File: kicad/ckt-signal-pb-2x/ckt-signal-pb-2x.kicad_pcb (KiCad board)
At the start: 2 copper layers, 25.8 x 66.7 mm, 15 parts, among them J1 Molex 0532610471, J2 Molex 0532610471

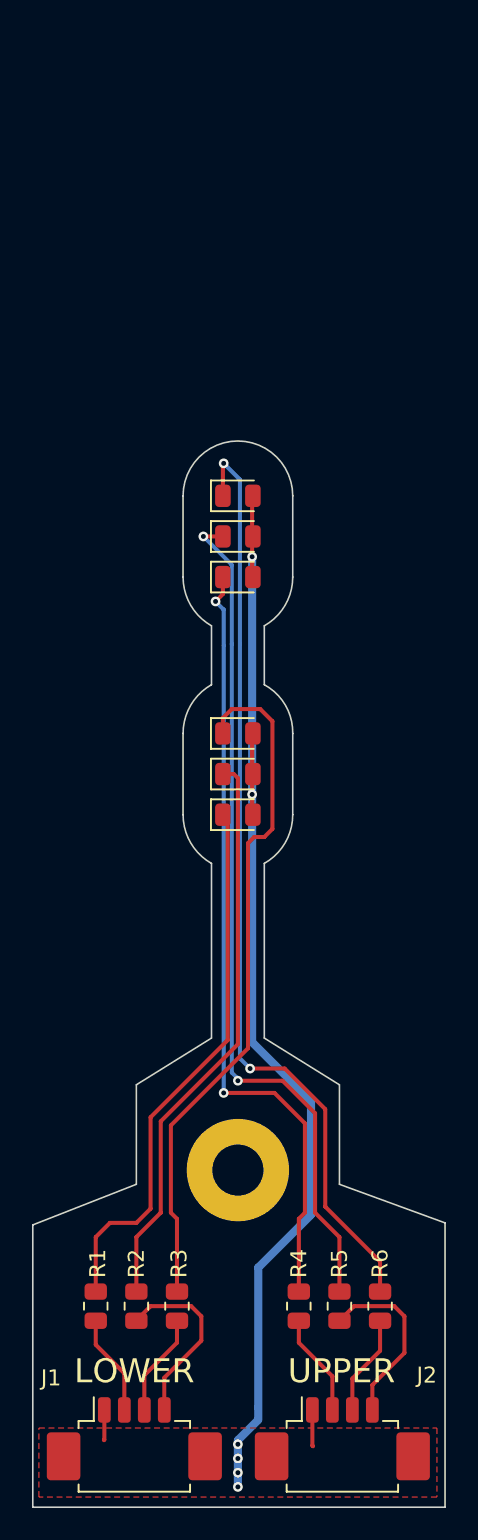
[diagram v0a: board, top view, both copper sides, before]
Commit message: Cleanup pcb, rename preference file
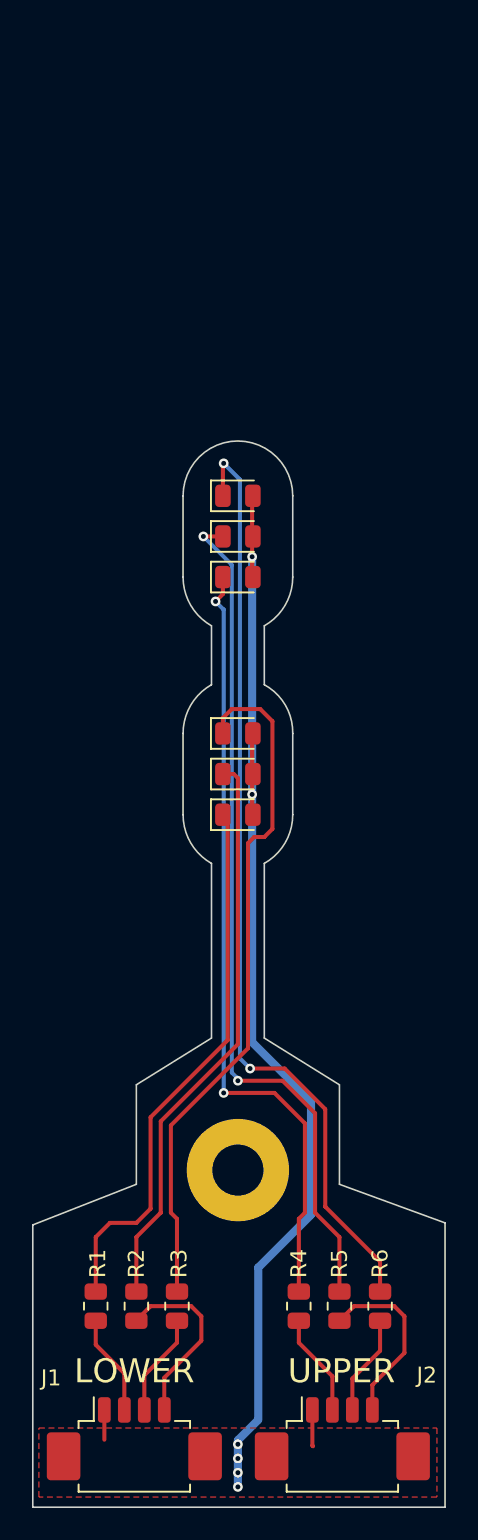
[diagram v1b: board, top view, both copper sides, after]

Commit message: Redesign 2x signal for better panelization
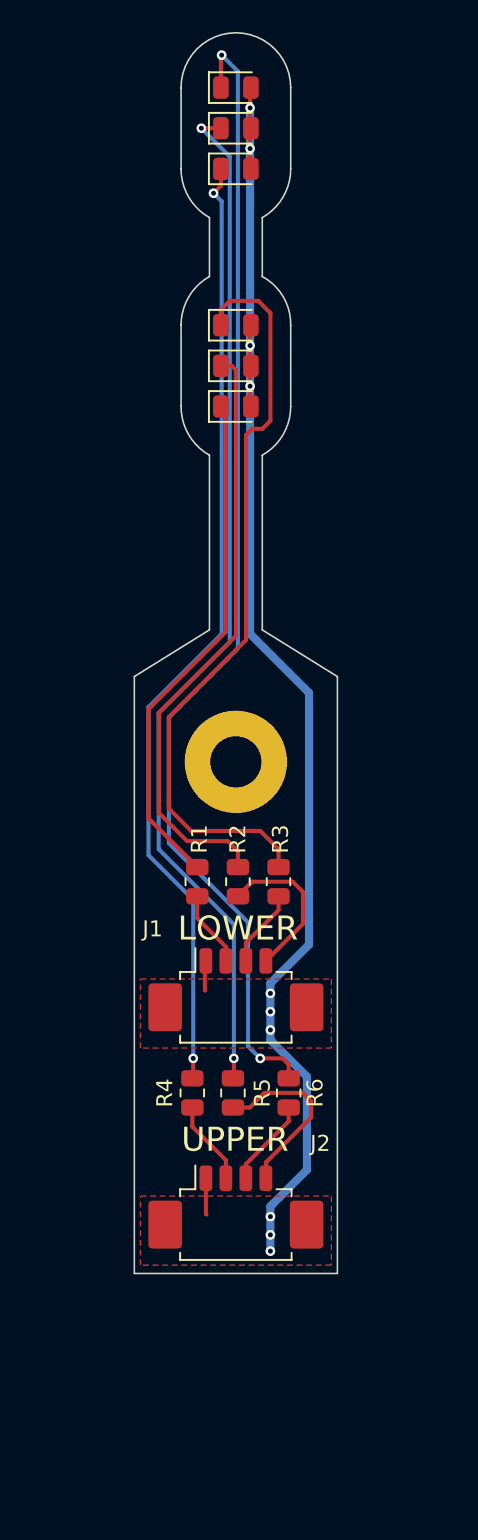
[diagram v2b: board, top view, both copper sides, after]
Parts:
- moved J1 28.8 mm to (32.3, 158.5)
- moved R1 27.3 mm to (29.8, 151.1)
- moved R2 27.3 mm to (32.4, 151.1)
- moved R3 27.3 mm to (34.9, 151.1)
- moved D3 25.5 mm to (32.3, 116.3)
- moved D4 25.5 mm to (32.3, 106.6)
- moved D2 25.5 mm to (32.3, 118.9)
- moved D6 25.5 mm to (32.3, 101.5)
- moved D1 25.5 mm to (32.3, 121.4)
- moved D5 25.5 mm to (32.3, 104.0)
- moved H1 25.5 mm to (32.3, 143.6)
- moved J2 15.9 mm to (32.3, 172.1)
- moved R4 14.9 mm to (29.5, 164.3)
- moved R5 14.9 mm to (32.1, 164.3)
- moved R6 14.5 mm to (35.6, 164.3)
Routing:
- net Net-(D1-Pad2): track 76.0 -> 90.3 mm, vias 6 -> 10
- net Net-(D6-Pad1): track 59.2 -> 72.2 mm
- net Net-(D5-Pad1): track 53.6 -> 65.2 mm
- net Net-(D4-Pad1): track 49.2 -> 60.3 mm
- net Net-(D3-Pad1): track 43.4 -> 47.6 mm
- net Net-(D1-Pad1): track 34.3 -> 32.2 mm
- net Net-(D2-Pad1): track 35.8 -> 37.7 mm
- net Net-(J1-Pad2): track 6.32 -> 4.78 mm
- net Net-(J1-Pad4): track 11.5 -> 10.00 mm
- net Net-(J1-Pad3): track 6.42 -> 4.89 mm
- net Net-(J2-Pad2): track 6.45 -> 5.29 mm
- net Net-(J2-Pad3): track 6.29 -> 5.53 mm
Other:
- board size 25.8 x 66.7 mm -> 12.7 x 77.6 mm
- board text added: "Iowa Scaled Engineering CKT-SIGNAL-PB-2X v3.0 ©2025 www.iascaled.com"
- board text removed: "Iowa Scaled Engineering CKT-SIGNAL-2X-PB v3.0 ©2025 www.iascaled.com"
